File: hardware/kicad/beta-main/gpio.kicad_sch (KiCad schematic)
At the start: 3 parts

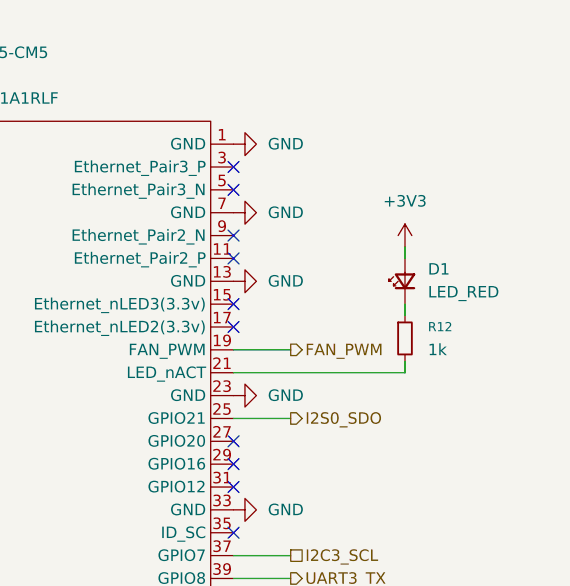
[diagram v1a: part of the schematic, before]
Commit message: BOM, all easily found parts from digi
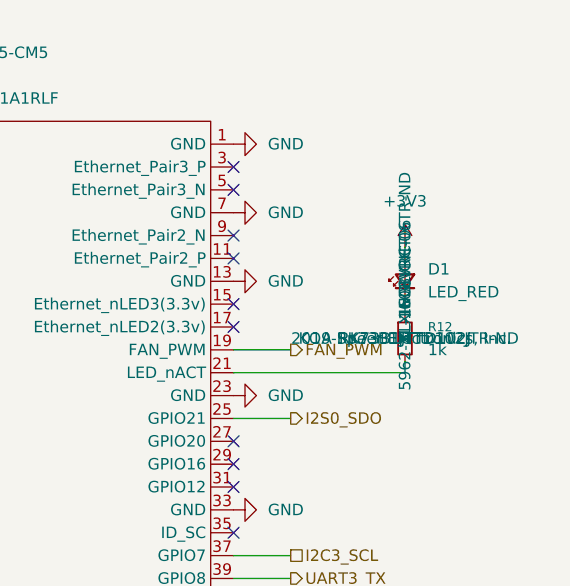
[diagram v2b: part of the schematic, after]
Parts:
- D1: DigiKey_Part_Number (none) -> 5962-XL-1608VRC-06TR-ND; MANUFACTURER (none) -> XINGLIGHT; MP (none) -> XL-1608VRC-06
- R12: DigiKey_Part_Number (none) -> 2019-RK73B1JTTD102JTR-ND; MANUFACTURER (none) -> KOA Speer Electronics, Inc.; MP (none) -> RK73B1JTTD102J
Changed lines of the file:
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@@
+			)
+		)
+		(property "DigiKey_Part_Number" "5962-XL-1608VRC-06TR-ND"
+			(at 148.59 59.69 0)
+			(effects
+				(font
+					(size 1.27 1.27)
+				)
+			)
+		)
+		(property "MANUFACTURER" "XINGLIGHT"
+			(at 148.59 59.69 0)
+			(effects
+				(font
+					(size 1.27 1.27)
+				)
+			)
+		)
+		(property "MP" "XL-1608VRC-06"
+			(at 148.59 59.69 0)
+			(effects
+				(font
+					(size 1.27 1.27)
+				)
 			)
 		)
@@
 			)
 		)
+		(property "DigiKey_Part_Number" "2019-RK73B1JTTD102JTR-ND"
+			(at 148.59 66.04 0)
+			(effects
+				(font
+					(size 1.27 1.27)
+				)
+			)
+		)
+		(property "MANUFACTURER" "KOA Speer Electronics, Inc."
+			(at 148.59 66.04 0)
+			(effects
+				(font
+					(size 1.27 1.27)
+				)
+			)
+		)
+		(property "MP" "RK73B1JTTD102J"
+			(at 148.59 66.04 0)
+			(effects
+				(font
+					(size 1.27 1.27)
+				)
+			)
+		)

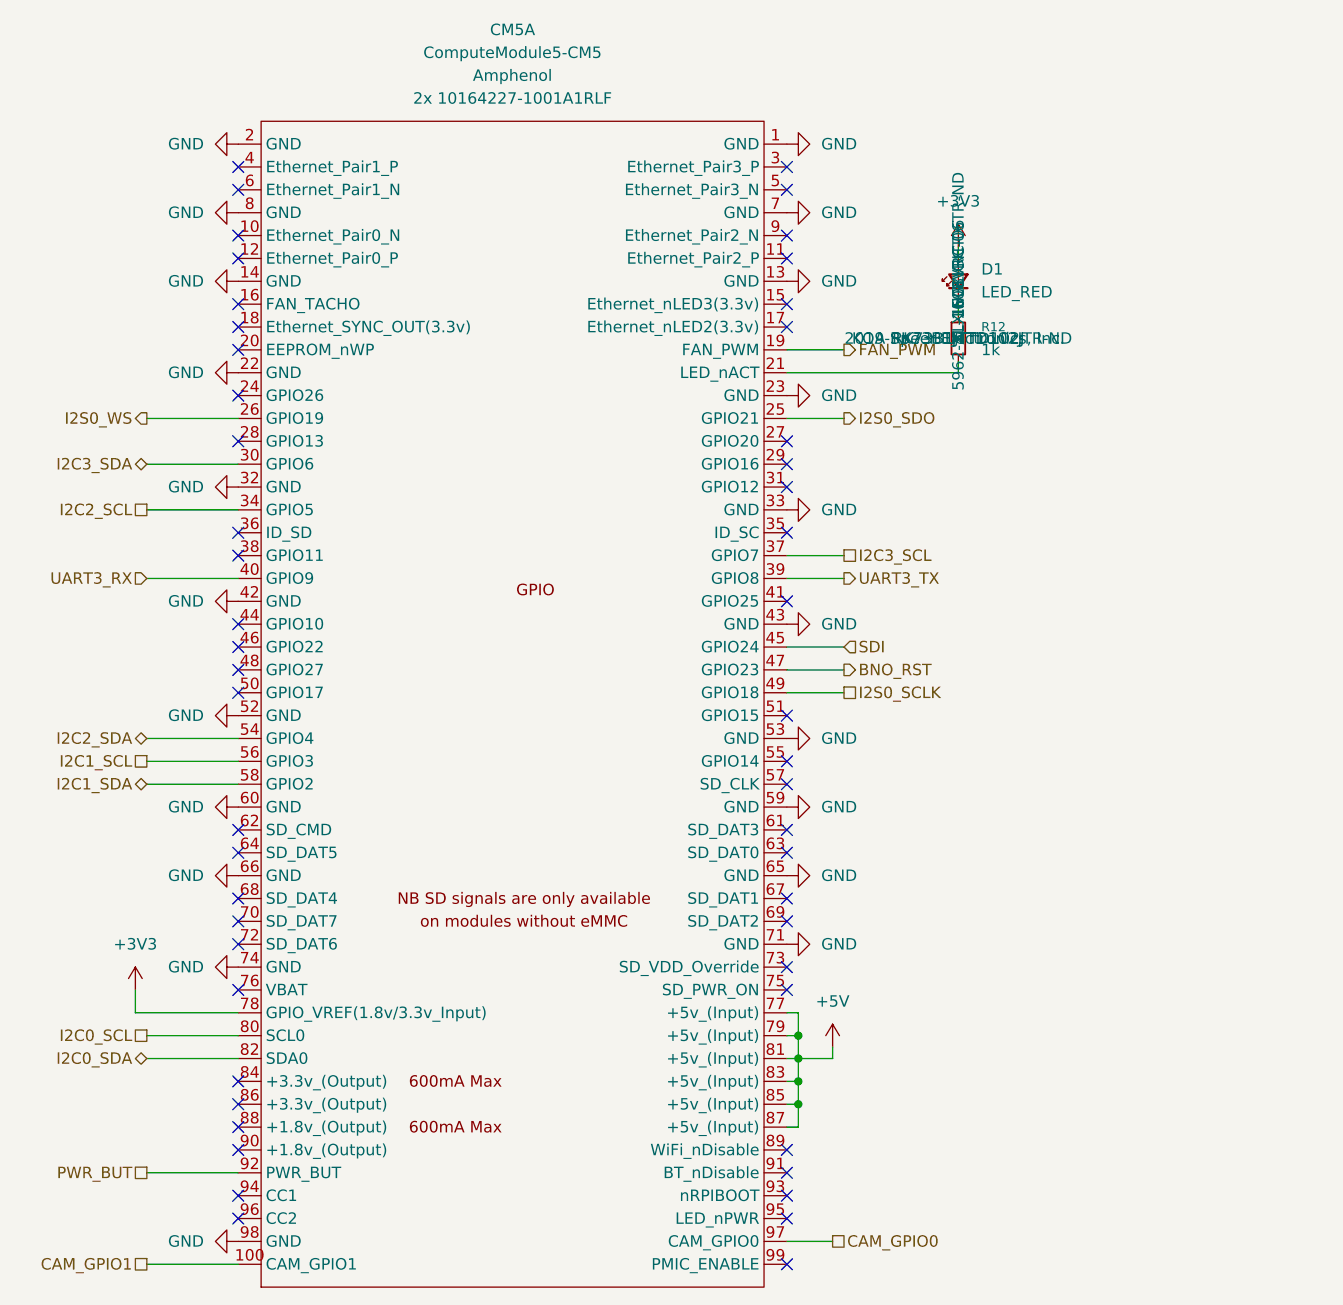
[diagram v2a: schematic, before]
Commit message: resolve DRC issues and generate fab files
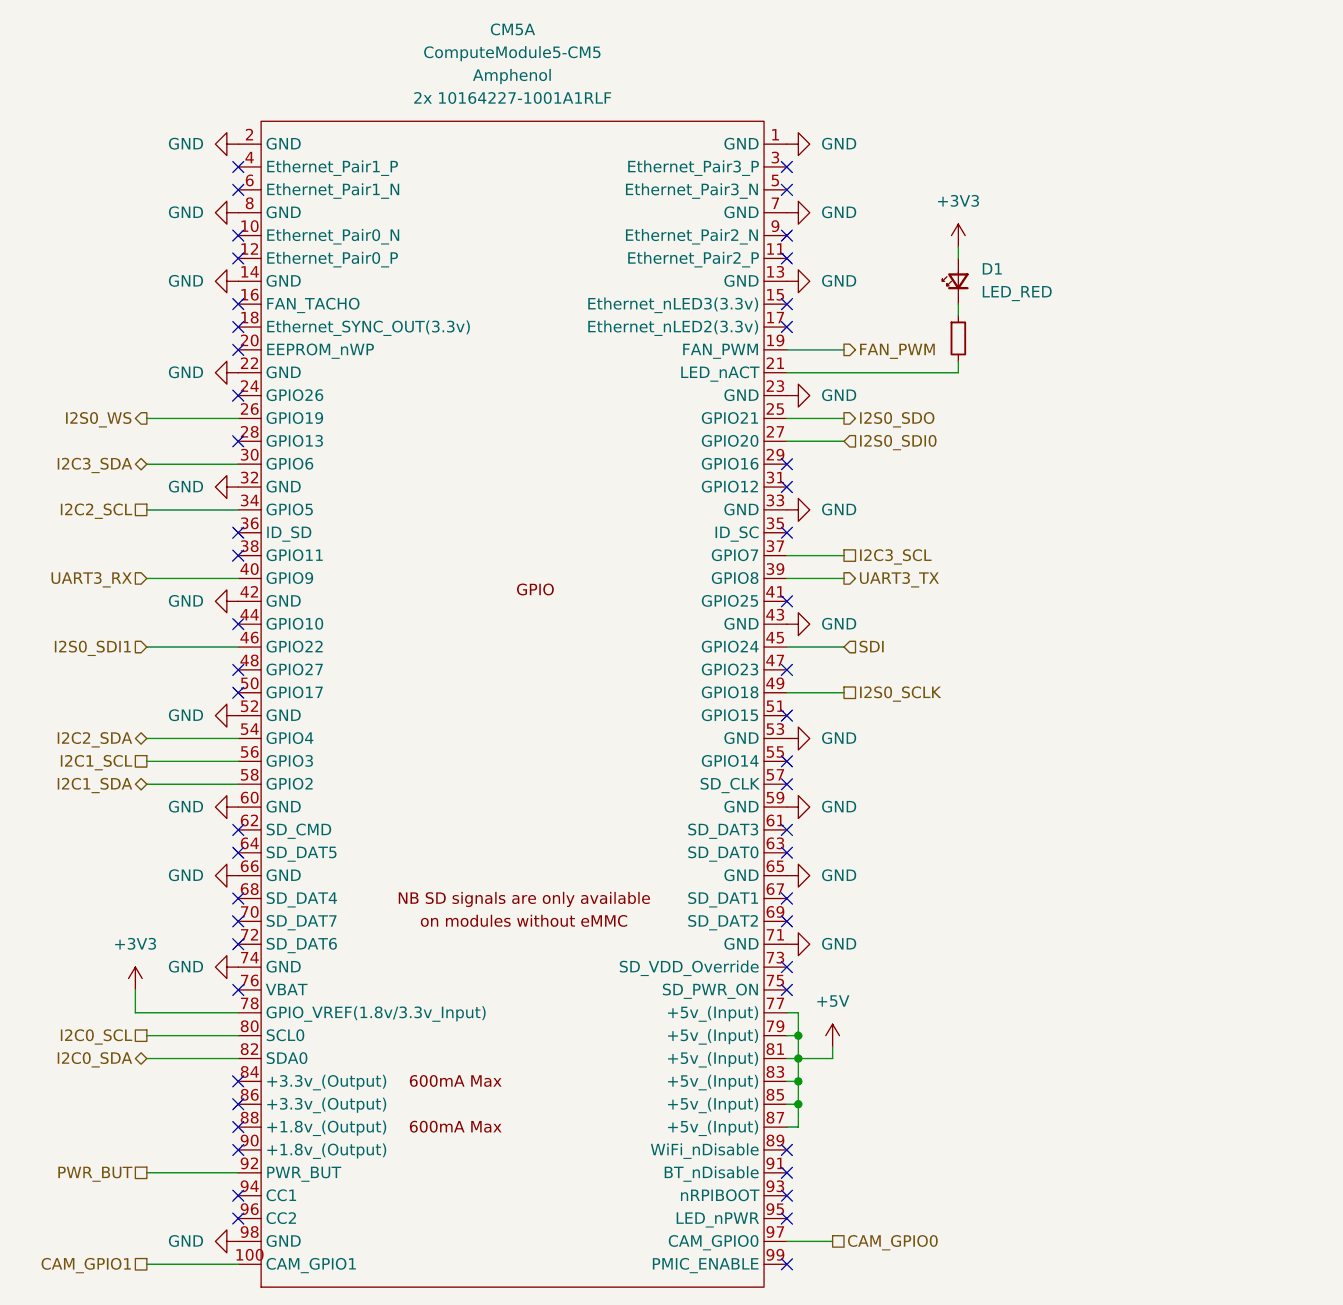
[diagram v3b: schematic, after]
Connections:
- net I2S0_SDI0: now reaches CM5.27 (GPIO20)
- net I2S0_SDI1: now reaches CM5.46 (GPIO22)
- net BNO_RST: no longer names the net of CM5.47 (GPIO23)
- no-connect marks 52 -> 51
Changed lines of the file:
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@@
-	)
-	(no_connect
-		(at 68.58 100.33)
 	)
 	(no_connect
@@
 	)
 	(no_connect
-		(at 129.54 77.47)
-	)
-	(no_connect
 		(at 129.54 46.99)
 	)
@@
 	)
 	(no_connect
+		(at 129.54 102.87)
+	)
+	(no_connect
 		(at 129.54 113.03)
 	)
@@
 	(wire
 		(pts
+			(xy 129.54 77.47) (xy 135.89 77.47)
+		)
+		(stroke
+			(width 0)
+			(type default)
+		)
+	)
+	(wire
+		(pts
+			(xy 58.42 100.33) (xy 68.58 100.33)
+		)
+		(stroke
+			(width 0)
+			(type default)
+		)
+	)
+	(wire
+		(pts
 			(xy 58.42 80.01) (xy 68.58 80.01)
 		)
@@
 		(pts
 			(xy 57.15 138.43) (xy 57.15 140.97)
-		)
-		(stroke
-			(width 0)
-			(type default)
-		)
-	)
-	(wire
-		(pts
-			(xy 129.54 102.87) (xy 135.89 102.87)
 		)
 		(stroke
@@
 		)
 	)
-	(hierarchical_label "BNO_RST"
-		(shape output)
-		(at 135.89 102.87 0)
-		(effects
-			(font
-				(size 1.27 1.27)
-			)
-			(justify left)
-		)
-	)
 	(hierarchical_label "I2S0_WS"
 		(shape output)
@@
 		)
 	)
+	(hierarchical_label "I2S0_SDI0"
+		(shape input)
+		(at 135.89 77.47 0)
+		(effects
+			(font
+				(size 1.27 1.27)
+			)
+			(justify left)
+		)
+	)
 	(hierarchical_label "I2C0_SDA"
 		(shape bidirectional)
 		(at 58.42 146.05 180)
+		(effects
+			(font
+				(size 1.27 1.27)
+			)
+			(justify right)
+		)
+	)
+	(hierarchical_label "I2S0_SDI1"
+		(shape input)
+		(at 58.42 100.33 180)
 		(effects
 			(font
@@
 			)
 		)
-		(property "Sim.Pins" ""
+		(property "Sim.Pins" "1=K 2=A"
 			(at 148.59 59.69 90)
 			(effects
@@
 					(size 1.27 1.27)
 				)
+				(hide yes)
 			)
 		)
@@
 					(size 1.27 1.27)
 				)
+				(hide yes)
 			)
 		)
@@
 					(size 1.27 1.27)
 				)
+				(hide yes)
 			)
 		)
@@
 				)
 				(justify left)
+				(hide yes)
 			)
 		)
@@
 				)
 				(justify left)
+				(hide yes)
 			)
 		)
@@
 					(size 1.27 1.27)
 				)
+				(hide yes)
 			)
 		)
@@
 					(size 1.27 1.27)
 				)
+				(hide yes)
 			)
 		)
@@
 					(size 1.27 1.27)
 				)
-			)
-		)
+				(hide yes)
+			)
+		)

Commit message: sync changes
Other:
- note added: "I2S0 I2C0 I2C1 I2C2 UART3"
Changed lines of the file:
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@@
 		(title "BETA MAIN BOARD - CM5 - GPIO")
+	)
+	(text "I2S0\n\nI2C0\nI2C1\nI2C2\n\nUART3"
+		(exclude_from_sim no)
+		(at 182.372 58.928 0)
+		(effects
+			(font
+				(size 2.54 2.54)
+			)
+		)
 	)
 	(junction

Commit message: add final touches, generate rev A fab and step files
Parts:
- R12: value 1k -> 100
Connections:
- net at D1.1 (K): now also R12.2; no longer R12.1
- net at CM5.21 (LED_nACT): now also R12.1; no longer R12.2
- net BATT_INT: now reaches CM5.55 (GPIO14)
- no-connect marks 51 -> 50
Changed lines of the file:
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@@
-	)
-	(no_connect
-		(at 129.54 113.03)
 	)
 	(no_connect
@@
 		(pts
 			(xy 134.62 146.05) (xy 134.62 144.78)
+		)
+		(stroke
+			(width 0)
+			(type default)
+		)
+	)
+	(wire
+		(pts
+			(xy 129.54 113.03) (xy 135.89 113.03)
 		)
 		(stroke
@@
 		(shape passive)
 		(at 135.89 90.17 0)
+		(effects
+			(font
+				(size 1.27 1.27)
+			)
+			(justify left)
+		)
+	)
+	(hierarchical_label "BATT_INT"
+		(shape input)
+		(at 135.89 113.03 0)
 		(effects
 			(font
@@
 		(lib_id "Device:R_Small")
 		(at 148.59 66.04 0)
+		(mirror x)
 		(unit 1)
 		(exclude_from_sim no)
@@
 		(on_board yes)
 		(dnp no)
-		(fields_autoplaced yes)
 		(property "Reference" "R12"
-			(at 151.13 64.7699 0)
+			(at 151.13 67.3101 0)
 			(effects
 				(font
@@
 				)
 				(justify left)
-				(hide yes)
-			)
-		)
-		(property "Value" "1k"
-			(at 151.13 67.3099 0)
+			)
+		)
+		(property "Value" "100"
+			(at 151.13 64.7701 0)
 			(effects
 				(font
@@
 				)
 				(justify left)
-				(hide yes)
-			)
-		)
+			)
+		)
